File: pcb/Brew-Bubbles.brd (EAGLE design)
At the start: 25.5 x 28.7 mm, 9 parts, among them U1 GP1A57HR, U2 WEMOS-D1-MINI

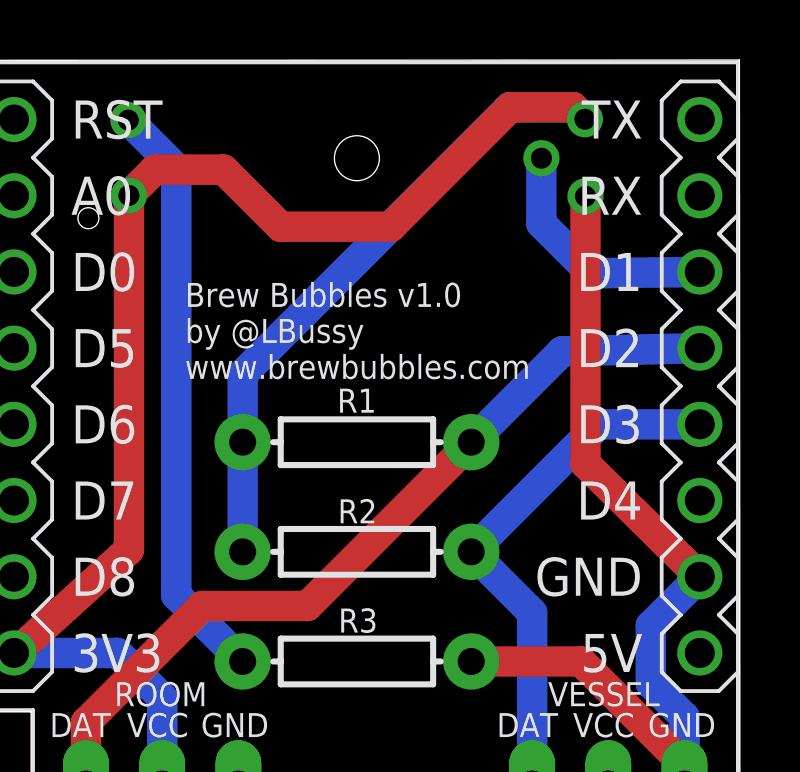
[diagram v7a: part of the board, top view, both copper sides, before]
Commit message: Add in decoupling cap for sensor
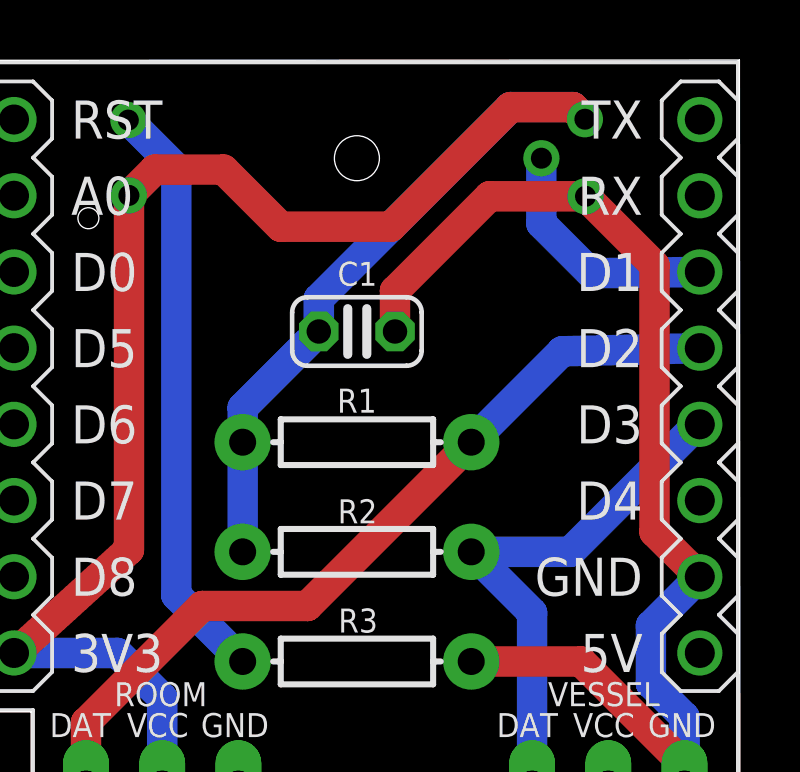
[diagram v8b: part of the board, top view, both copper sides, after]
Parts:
- added C1: 0.1μF, rcl:C025-024X044
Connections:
- net 3V3: now also C1.1
- net GND: now also C1.2
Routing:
- net GND: track 51.2 -> 60.2 mm
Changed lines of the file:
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@@
 <wire x1="1.94" y1="0.03" x2="25.57" y2="0.03" width="0" layer="20"/>
 <wire x1="0.03" y1="28.74" x2="25.55" y2="28.75" width="0" layer="20"/>
-<text x="7.06840625" y="18.12" size="0.8" layer="25" font="vector" ratio="14">Brew Bubbles v1.0
+<text x="14.51145" y="5.72" size="0.8" layer="26" font="vector" ratio="14" rot="MR90" align="top-left">Brew Bubbles v1.0
 by @LBussy
 www.brewbubbles.com</text>
@@
 <attribute name="POPULARITY" value="17" x="21.18" y="0.74" size="1.778" layer="28" rot="MR180" display="off"/>
 </element>
+<element name="C1" library="rcl" library_urn="urn:adsk.eagle:library:334" package="C025-024X044" package3d_urn="urn:adsk.eagle:package:23630/1" value="0.1μF" x="12.8" y="19.7" smashed="yes">
+<attribute name="NAME" x="12.814" y="21.224" size="0.8" layer="25" ratio="10" align="bottom-center"/>
+<attribute name="POPULARITY" value="56" x="12.8" y="19.7" size="1.778" layer="27" display="off"/>
+<attribute name="SPICEPREFIX" value="C" x="12.8" y="19.7" size="1.778" layer="27" display="off"/>
+</element>
 </elements>
 <signals>
@@
 <contactref element="U1" pad="5"/>
 <wire x1="24.23" y1="11.525" x2="24.23" y2="11.525696875" width="1.016" layer="1"/>
-<wire x1="24.23" y1="11.525696875" x2="20.42" y2="15.291496875" width="1.016" layer="1"/>
-<wire x1="20.42" y1="15.291496875" x2="20.42" y2="24.2062" width="1.016" layer="1"/>
+<wire x1="24.23" y1="11.525696875" x2="22.72" y2="13.018178125" width="1.016" layer="1"/>
+<wire x1="22.72" y1="21.9062" x2="20.42" y2="24.2062" width="1.016" layer="1"/>
+<wire x1="22.72" y1="21.9062" x2="22.72" y2="13.018178125" width="1.016" layer="1"/>
 <wire x1="22.6" y1="7.97" x2="23.72" y2="6.85" width="1.016" layer="16"/>
 <wire x1="22.6" y1="9.895" x2="24.23" y2="11.525" width="1.016" layer="16"/>
@@
 <contactref element="ROOM" pad="1"/>
 <wire x1="8.85" y1="2.65" x2="8.85" y2="4.55" width="1.016" layer="16"/>
+<contactref element="C1" pad="2"/>
+<wire x1="17.22" y1="24.2062" x2="14.07" y2="21.0562" width="1.016" layer="1"/>
+<wire x1="17.22" y1="24.2062" x2="20.42" y2="24.2062" width="1.016" layer="1"/>
+<wire x1="14.07" y1="19.7" x2="14.07" y2="21.0562" width="1.016" layer="1"/>
 </signal>
 <signal name="3V3">
@@
 <contactref element="R2" pad="P$2"/>
 <contactref element="R1" pad="P$2"/>
-<wire x1="17.8894" y1="27.1762" x2="8.9913" y2="18.2781" width="1.016" layer="16"/>
-<wire x1="8.9913" y1="16.01" x2="8.9913" y2="18.2781" width="1.016" layer="16"/>
-<wire x1="20" y1="27.1762" x2="20.4" y2="26.7762" width="1.016" layer="16"/>
-<wire x1="20" y1="27.1762" x2="17.8894" y2="27.1762" width="1.016" layer="16"/>
 <wire x1="5.2" y1="24.2362" x2="5.2" y2="12.42035" width="1.016" layer="1"/>
 <wire x1="5.2" y1="12.42035" x2="1.37383125" y2="8.9408" width="1.016" layer="1"/>
@@
 <wire x1="8.3556" y1="25.0962" x2="10.2588" y2="23.193" width="1.016" layer="1"/>
 <wire x1="10.2588" y1="23.193" x2="13.933" y2="23.193" width="1.016" layer="1"/>
-<wire x1="20" y1="27.1762" x2="20.4" y2="26.7762" width="1.016" layer="1"/>
 <wire x1="20" y1="27.1762" x2="17.9162" y2="27.1762" width="1.016" layer="1"/>
 <wire x1="13.933" y1="23.193" x2="17.9162" y2="27.1762" width="1.016" layer="1"/>
@@
 <wire x1="6.31" y1="7.49" x2="6.31" y2="4.55" width="1.016" layer="16"/>
 <wire x1="4.815" y1="8.985" x2="6.31" y2="7.49" width="1.016" layer="16"/>
+<contactref element="C1" pad="1"/>
+<wire x1="20.4" y1="26.7762" x2="20" y2="27.1762" width="1.016" layer="1"/>
+<wire x1="8.9913" y1="16.01" x2="8.9913" y2="17.1613" width="1.016" layer="16"/>
+<wire x1="8.9913" y1="17.1613" x2="11.53" y2="19.7" width="1.016" layer="16"/>
+<wire x1="11.53" y1="19.7" x2="11.53" y2="20.79" width="1.016" layer="16"/>
+<wire x1="11.53" y1="20.79" x2="17.92" y2="27.18" width="1.016" layer="16"/>
+<wire x1="17.92" y1="27.18" x2="19.9962" y2="27.18" width="1.016" layer="16"/>
+<wire x1="19.9962" y1="27.18" x2="20.4" y2="26.7762" width="1.016" layer="16"/>
 </signal>
 <signal name="D2">
@@
 <signal name="D3">
 <contactref element="U2" pad="JP2.5"/>
-<wire x1="20.8609" y1="16.605" x2="24.23" y2="16.605" width="1.016" layer="16"/>
+<wire x1="24.1609" y1="16.605" x2="24.23" y2="16.605" width="1.016" layer="16"/>
 <contactref element="R2" pad="P$1"/>
 <contactref element="VESSEL" pad="3"/>
 <wire x1="18.64" y1="4.55" x2="18.64" y2="10.3267" width="1.016" layer="16"/>
 <wire x1="18.64" y1="10.3267" x2="16.6113" y2="12.3554" width="1.016" layer="16"/>
-<wire x1="16.6113" y1="12.3554" x2="20.8609" y2="16.605" width="1.016" layer="16"/>
+<wire x1="16.6113" y1="12.3554" x2="19.9113" y2="12.3554" width="1.016" layer="16"/>
+<wire x1="24.1609" y1="16.605" x2="19.9113" y2="12.3554" width="1.016" layer="16"/>
 </signal>
 <signal name="D1">
